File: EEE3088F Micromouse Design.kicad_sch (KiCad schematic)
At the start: 4 parts, among them J1 Conn_02x16_Odd_Even, J2 Conn_01x02, U1 INA219AxD

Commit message: Added DRV8837 Motor Driver x4. Footprint PCB Organisation outstanding
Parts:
- added C10, C11, C12, C13, C2, C3, C4, C5, C6, C7, C8, C9: 0.1mF, Capacitor_SMD:C_0402_1005Metric_Pad0.74x0.62mm_HandSolder, symbol Device:C_Small
- added U2, U3, U4, U5: DRV8837, Package_SON:WSON-8-1EP_2x2mm_P0.5mm_EP0.9x1.6mm, symbol Driver_Motor:DRV8837
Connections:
- net GND: now also C10.1, C11.2, C12.2, C13.1, C2.2, C3.2, C4.1, C5.2, C6.2, C7.1, C8.2, C9.2, U2.4 (GND), U2.8 (VCC), U2.9 (GND), U3.4 (GND), U3.8 (VCC), U3.9 (GND), U4.4 (GND), U4.8 (VCC), U4.9 (GND), U5.4 (GND), U5.8 (VCC), U5.9 (GND)
- net Motor2_B_OUT: now reaches J1.1 (Pin_1)
- net Motor2_B_OUT: now also U3.3 (OUT2)
- net MOTOR4_CTRL2: now reaches J1.10 (Pin_10)
- net MOTOR4_CTRL2: now also U5.5 (IN2)
- net Motor2_A_OUT: now reaches J1.2 (Pin_2)
- net Motor2_A_OUT: now also U3.2 (OUT1)
- net 5V Out: now reaches J1.20 (Pin_20)
- net 5V Out: now also C11.1, C3.1, C5.1, C8.1, U2.7 (~{SLEEP}), U3.7 (~{SLEEP}), U4.7 (~{SLEEP}), U5.7 (~{SLEEP})
- net MOTOR3_CTRL1: now reaches J1.24 (Pin_24)
- net MOTOR3_CTRL1: now also U4.6 (IN1)
- net MOTOR3_CTRL2: now reaches J1.26 (Pin_26)
- net MOTOR3_CTRL2: now also U4.5 (IN2)
- net MOTOR3_A_OUT: now reaches J1.27 (Pin_27)
- net MOTOR3_A_OUT: now also U4.2 (OUT1)
- net MOTOR1_CTRL1: now reaches J1.28 (Pin_28)
- net MOTOR1_CTRL1: now also U2.6 (IN1)
- net MOTOR3_B_OUT: now reaches J1.29 (Pin_29)
- net MOTOR3_B_OUT: now also U4.3 (OUT2)
- net Motor4_A_OUT: now reaches J1.3 (Pin_3)
- net Motor4_A_OUT: now also U5.2 (OUT1)
- net MOTOR1_CTRL2: now reaches J1.30 (Pin_30)
- net MOTOR1_CTRL2: now also U2.5 (IN2)
- net MOTOR1_B_OUT: now reaches J1.31 (Pin_31)
- net MOTOR1_B_OUT: now also U2.3 (OUT2)
- net MOTOR1_A_OUT: now reaches J1.32 (Pin_32)
- net MOTOR1_A_OUT: now also U2.2 (OUT1)
- net MOTOR2_CTRL1: now reaches J1.4 (Pin_4)
- net MOTOR2_CTRL1: now also U3.6 (IN1)
- net Motor4_B_OUT: now reaches J1.5 (Pin_5)
- net Motor4_B_OUT: now also U5.3 (OUT2)
- net MOTOR2_CTRL2: now reaches J1.6 (Pin_6)
- net MOTOR2_CTRL2: now also U3.5 (IN2)
- net MOTOR4_CTRL1: now reaches J1.8 (Pin_8)
- net MOTOR4_CTRL1: now also U5.6 (IN1)
- new net 3.3V Regulated: C10.2, C13.2, C4.2, C7.2, U2.1 (VM), U3.1 (VM), U4.1 (VM), U5.1 (VM)
- new net Motor_H_Supply: C12.1, C2.1, C6.1, C9.1
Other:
- moved on the sheet: J1, J2, R1, U1

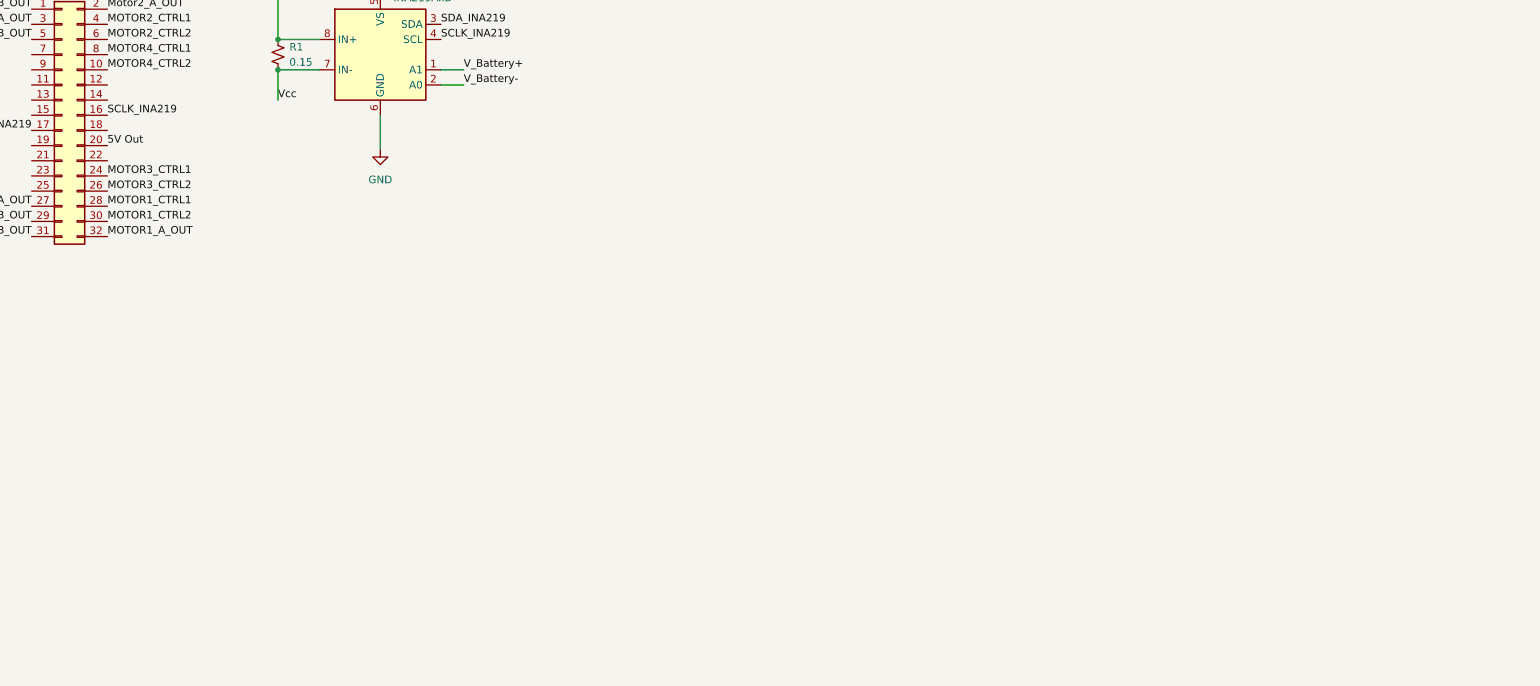
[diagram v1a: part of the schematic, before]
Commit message: Added 3.3V and 5V outputs
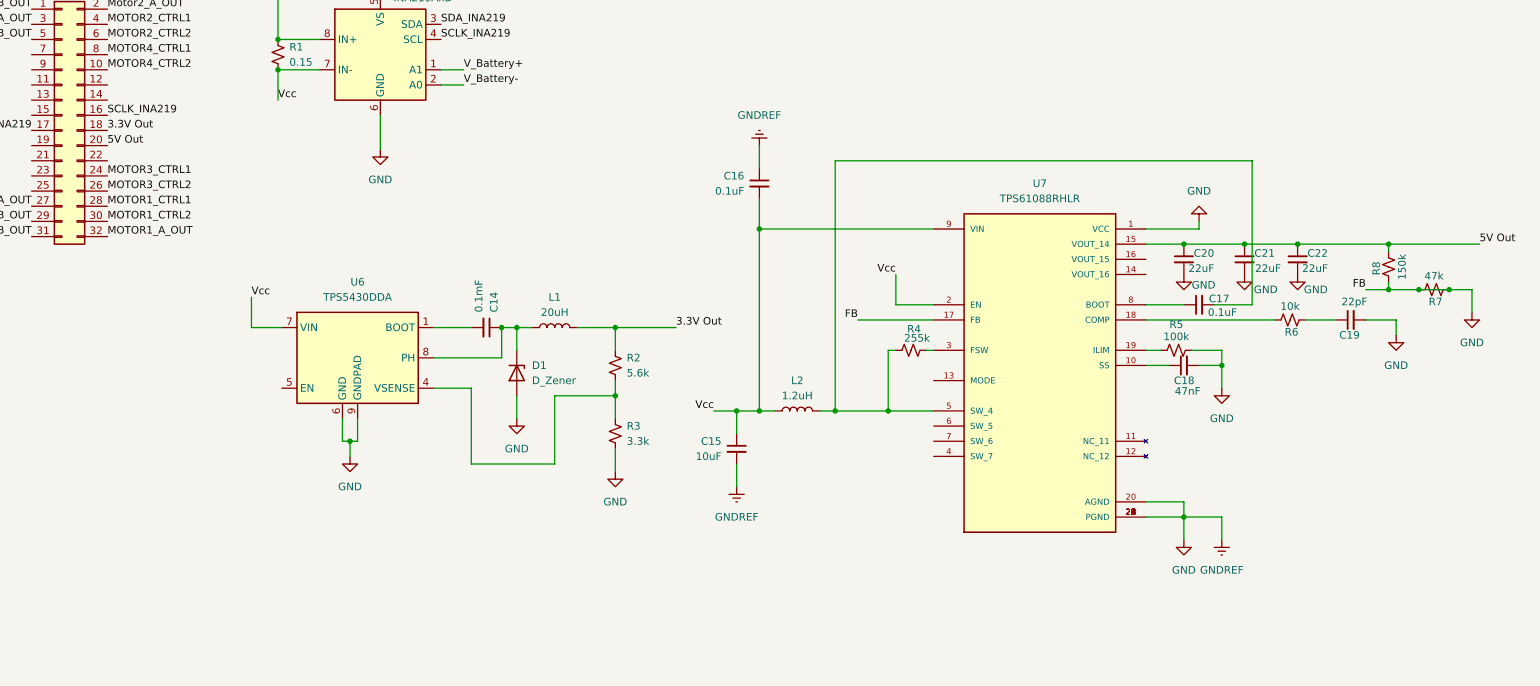
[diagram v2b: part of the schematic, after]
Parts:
- added C14: 0.1mF, Capacitor_SMD:C_0402_1005Metric_Pad0.74x0.62mm_HandSolder, symbol Device:C_Small
- added C15: 10uF, Capacitor_SMD:C_0402_1005Metric_Pad0.74x0.62mm_HandSolder, symbol Device:C_Small
- added C16, C17: 0.1uF, Capacitor_SMD:C_0402_1005Metric_Pad0.74x0.62mm_HandSolder, symbol Device:C_Small
- added C18: 47nF, Capacitor_SMD:C_0402_1005Metric_Pad0.74x0.62mm_HandSolder, symbol Device:C_Small
- added C19: 22pF, Capacitor_SMD:C_0402_1005Metric_Pad0.74x0.62mm_HandSolder, symbol Device:C_Small
- added C20, C21, C22: 22uF, Capacitor_SMD:C_0402_1005Metric_Pad0.74x0.62mm_HandSolder, symbol Device:C_Small
- added D1: D_Zener, symbol Device:D_Zener
- added L1: 20uH, symbol Device:L
- added L2: 1.2uH, symbol Device:L
- added R2: 5.6k, Resistor_SMD:R_1206_3216Metric_Pad1.30x1.75mm_HandSolder, symbol Device:R_Small_US
- added R3: 3.3k, Resistor_SMD:R_1206_3216Metric_Pad1.30x1.75mm_HandSolder, symbol Device:R_Small_US
- added R4: 255k, Resistor_SMD:R_1206_3216Metric_Pad1.30x1.75mm_HandSolder, symbol Device:R_Small_US
- added R5: 100k, Resistor_SMD:R_1206_3216Metric_Pad1.30x1.75mm_HandSolder, symbol Device:R_Small_US
- added R6: 10k, Resistor_SMD:R_1206_3216Metric_Pad1.30x1.75mm_HandSolder, symbol Device:R_Small_US
- added R7: 47k, Resistor_SMD:R_1206_3216Metric_Pad1.30x1.75mm_HandSolder, symbol Device:R_Small_US
- added R8: 150k, Resistor_SMD:R_1206_3216Metric_Pad1.30x1.75mm_HandSolder, symbol Device:R_Small_US
- added U6: TPS5430DDA, Package_SO:TI_SO-PowerPAD-8_ThermalVias, symbol Regulator_Switching:TPS5430DDA
- added U7: TPS61088RHLR, TPS61088RHLR:IC_TPS61088RHLR, symbol TPS61088RHLR:TPS61088RHLR
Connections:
- net 5V Out: now also C20.1, C21.1, C22.1, R8.2, U7.15 (VOUT_14)
- net GND: now also C15.2, C16.1, C18.2, C19.2, C20.2, C21.2, C22.2, D1.2 (A), R3.1, R5.1, R7.1, R7.2, R8.1, U6.6 (GND), U6.9 (GNDPAD), U7.1 (VCC), U7.17 (FB), U7.20 (AGND), U7.21 (PGND), U7.22 (PGND), U7.23 (PGND), U7.24 (PGND), U7.25 (PGND), U7.26 (PGND), U7.27 (PGND), U7.28 (PGND), U7.29 (PGND)
- net Vcc: now also C15.1, C16.2, L2.1, U6.7 (VIN), U7.2 (EN), U7.9 (VIN)
- net 3.3V Out: now reaches J1.18 (Pin_18)
- net 3.3V Out: now also L1.2, R2.2
- new net: C14.1, D1.1 (K), L1.1, U6.8 (PH)
- new net: C17.1, U7.8 (BOOT)
- new net: C17.2, L2.2, R4.2, U7.5 (SW_4)
- new net: R4.1, U7.3 (FSW)
- new net: R2.1, R3.2, U6.4 (VSENSE)
- new net: C18.1, U7.10 (SS)
- new net: R6.2, U7.18 (COMP)
- new net: R5.2, U7.19 (ILIM)
- new net: C14.2, U6.1 (BOOT)
- new net: C19.1, R6.1

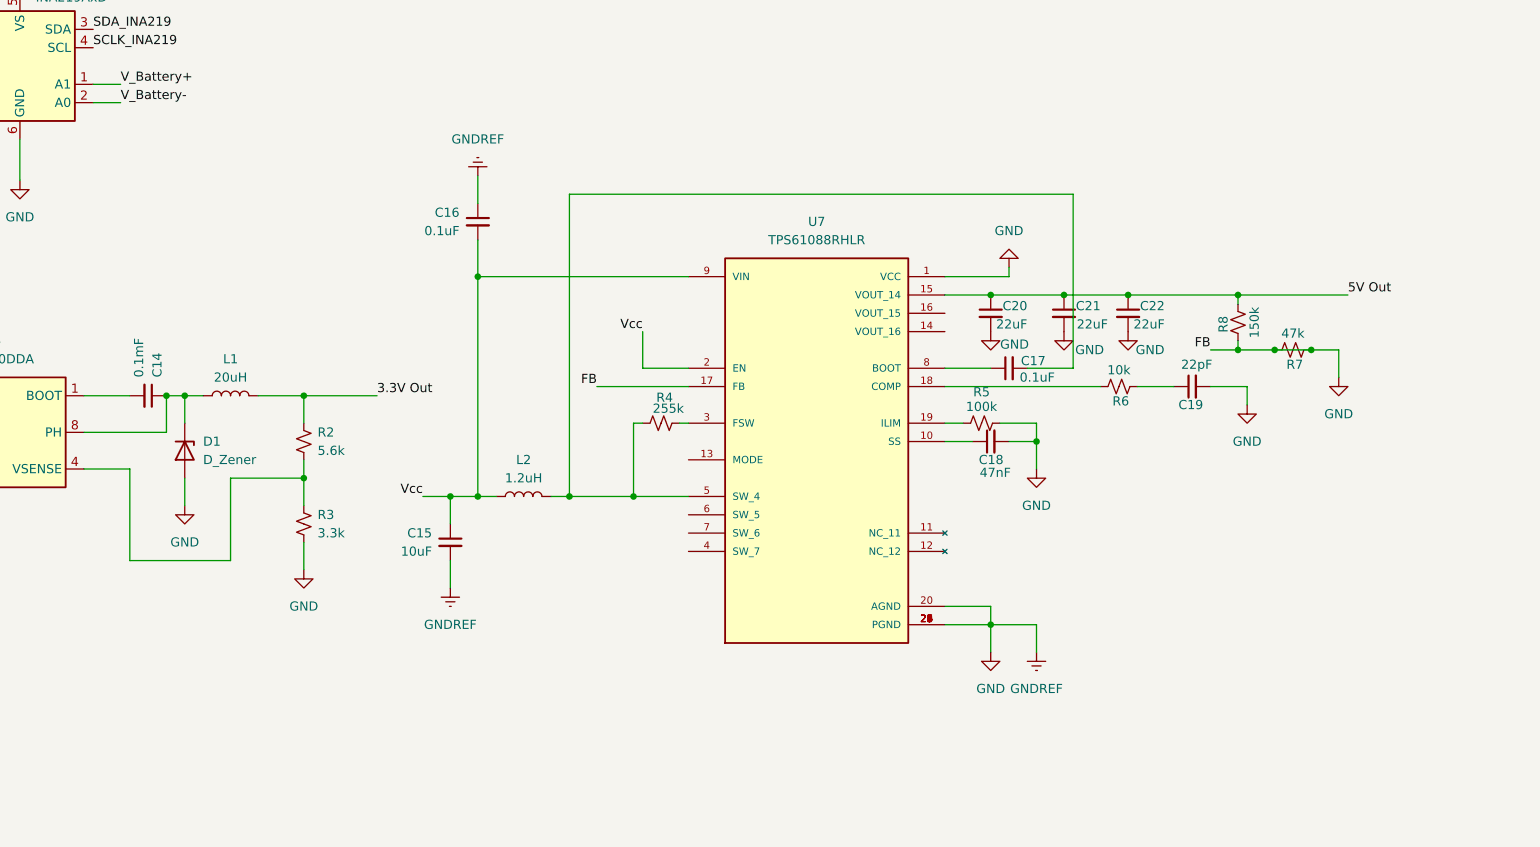
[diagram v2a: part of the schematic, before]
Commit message: Minor change to voltage regulator
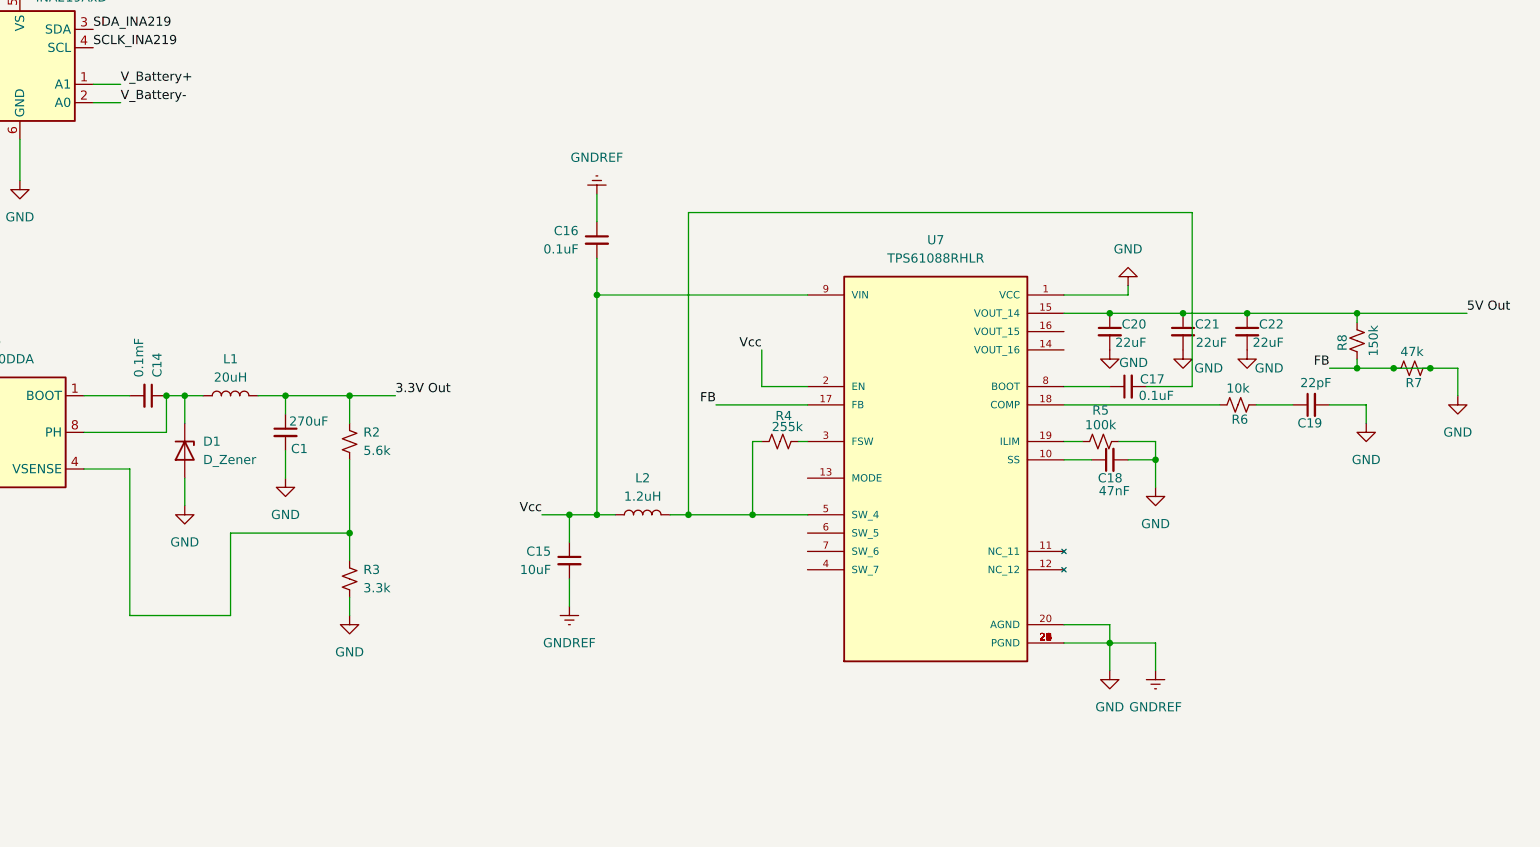
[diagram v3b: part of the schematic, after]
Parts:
- added C1: 270uF, symbol Device:C_Small
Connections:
- net 3.3V Out: now also C1.1
- net GND: now also C1.2
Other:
- moved on the sheet: C15, C16, C17, C18, C19, C20, C21, C22, L2, R2, R3, R4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
